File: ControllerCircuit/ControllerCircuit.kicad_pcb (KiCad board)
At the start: 2 copper layers, 122.5 x 87.5 mm, 89 parts, among them J1 ScrewTerminal, J10 Conn_01x02_Female, J11 Conn_01x03_Female, J12 ScrewTerminal, J13 Conn_01x03_Female, J14 Receive, J2 ScrewTerminal3Pin, J3 ScrewTerminal3Pin, J4 ScrewTerminal, J5 ScrewTerminal, J6 AVR-ISP-6, J7 ScrewTerminal, J8 2x3 2.54mm IDC Connectors, J9 Conn_01x06_Female, K1 SRD-05VDC-SL-C, K2 SRD-05VDC-SL-C, Q1 AO3400A, Q2 AO3400A, Q3 AO3401A, SW1 PTS645SL50-2LFS, U1 TJA1051T/3, U10 ATtiny841-SSU, U11 MicroSD_SPI_CD, U12 AQY212GSZ, U2 EL3H7(B)(TA)-G, U3 TCA6408AQPWRQ1, U4 ESP32-DEVKITC-32D, U5 SN65HVD75DR, U6 AMS1117-3.3, U8 TCA9534A, U9 AQY212GSZ

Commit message: Move LEDs near relays (improve seperation)
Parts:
- added G***: LOGO, ControllerCircuit:diode_symbol, F.Cu at (158.7, 74.2)
- added G***: LOGO, ControllerCircuit:diode_symbol, F.Cu at (149.1, 72.1)
- added G***: LOGO, ControllerCircuit:diode_symbol, F.Cu at (201.9, 74.9)
- added G***: LOGO, ControllerCircuit:diode_symbol, F.Cu at (200.7, 53.8)
- added G***: LOGO, ControllerCircuit:diode_symbol, F.Cu at (147.9, 53.7)
- moved R12 36.6 mm to (208.3, 76.1), turned to 180 degrees
- moved D3 19.5 mm to (198.6, 53.6), turned to 90 degrees
- moved R13 6.10 mm to (152.6, 52.9)
- moved D4 1.97 mm to (145.8, 53.6), turned to 90 degrees
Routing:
- net Net-(D3-Pad2): track 4.07 -> 33.2 mm
- net Net-(D2-Pad2): track 49.0 -> 24.2 mm
- net FUSED5V: track 299.4 -> 275.7 mm
- net Net-(D4-Pad1): track 26.8 -> 28.7 mm
- net Net-(D4-Pad2): track 4.45 -> 5.95 mm
- net GND: vias 243 -> 246
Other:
- outline, holes or cut-outs redrawn

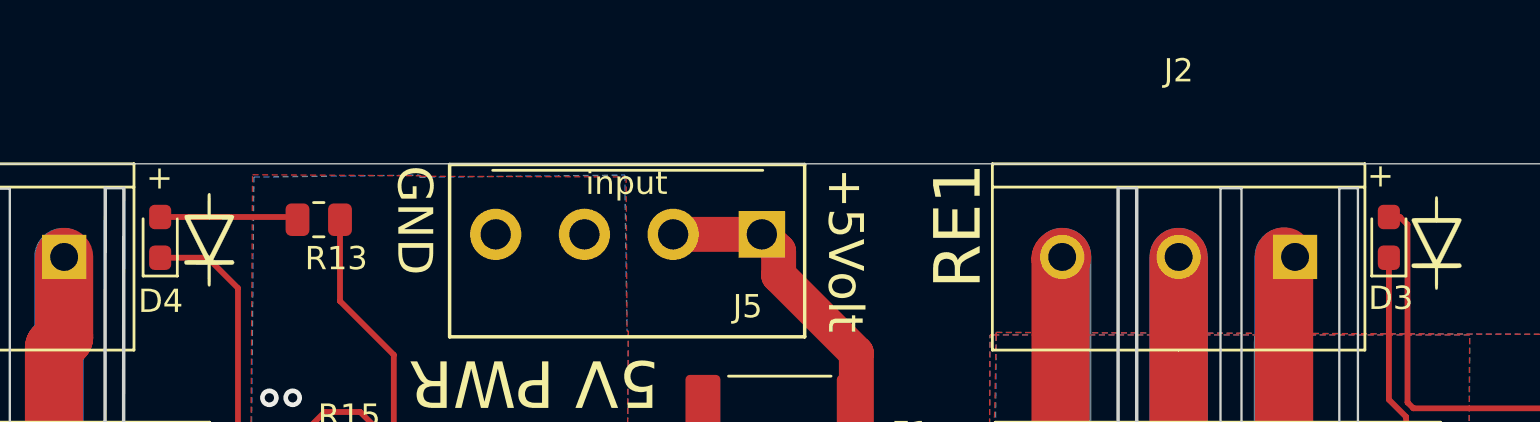
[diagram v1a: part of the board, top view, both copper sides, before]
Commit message: Updated Patreon list on silkscreen
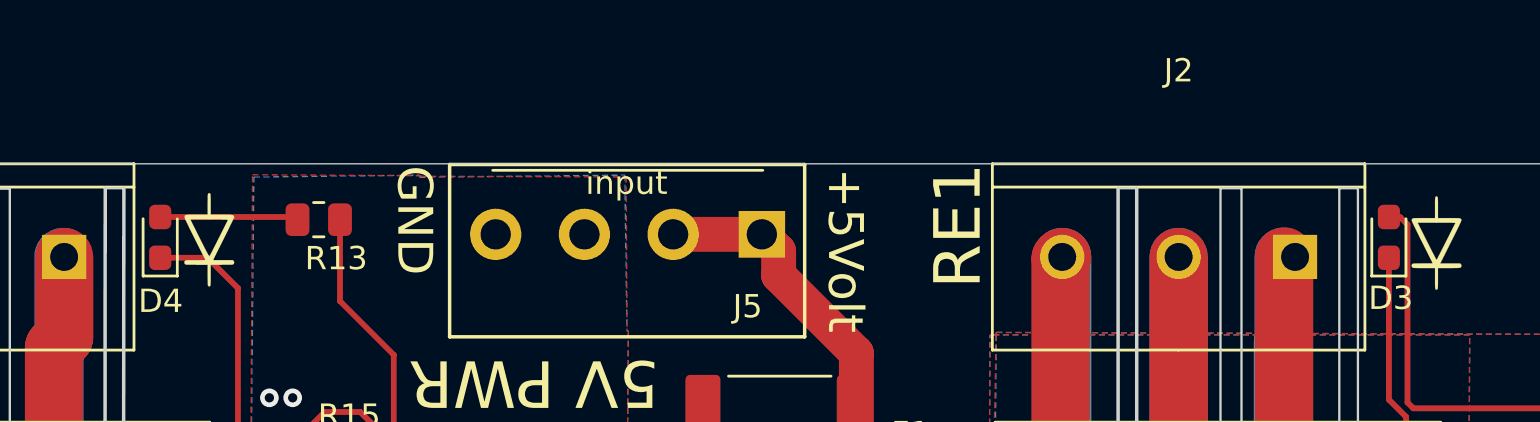
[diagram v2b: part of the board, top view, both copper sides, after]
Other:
- board text added: "IronXSide, Pawel S, Luke Anderson Mukunda Modell, Ken Lyman DIY Solar Energy, Jaanus Marko Kranjcic, Ross Mitchell Micah Peterson, Sebastian M Tim Yorba, chapulino1000 Tudor Bogdan Teodorescu manuromero05, Patrick Murphy Juan Matos, Nico F Arkadiusz Poscik, Marco Martin Bogomolni Julius Pabrinkis Constantine Macris Jose Cruz, Buenaventura Satorra Juanmijm, Thomas W Alberto Santos, Chad Artiaga Th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"
- board text added: "https://github.com/stuartpittaway/diyBMSv4"
- board text removed: "Arkadiusz Poscik, Marco Martin Bogomolni Julius Pabrinkis, Patrick Murphy Constantine Macris Jose Cruz, Juanmijm Buenaventura Satorra Thomas W, Alberto Santos Chad Artiaga, Thales of Miletus manuromero05, Julian Cox"
- board text removed: "IronXSide Pawel S Luke Anderson Mukunda Modell Adam Davis, Ken Lyman DIY Solar Energy Jaanus, Marko Kranjcic Ross Mitchell, Micah Peterson Sebastian M, chapulino1000 Tudor Bogdan Teodorescu Manuel Romero, Tim Yorba Juan Matos, Nico F"
- board text removed: "github.com/stuartpittaway/diyBMSv4Hardware"
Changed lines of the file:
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@@
   (general
     (thickness 1.6)
-    (drawings 188)
+    (drawings 185)
     (tracks 1521)
     (zones 0)
@@
     (34 B.Paste user hide)
     (35 F.Paste user hide)
-    (36 B.SilkS user hide)
+    (36 B.SilkS user)
     (37 F.SilkS user)
     (38 B.Mask user hide)
@@
   (gr_line (start 180.53 78.78) (end 201.99 78.78) (layer B.SilkS) (width 0.12))
   (gr_line (start 180.53 50.8) (end 180.53 78.78) (layer B.SilkS) (width 0.12))
-  (gr_text "Arkadiusz Poscik, Marco\nMartin Bogomolni\n\n\nJulius Pabrinkis, Patrick Murphy\nConstantine Macris\n\n\nJose Cruz, Juanmijm\nBuenaventura Satorra\nThomas W, Alberto Santos\nChad Artiaga, Thales of Miletus\nmanuromero05, Julian Cox" (at 183.7 101.7 90) (layer B.SilkS)
-    (effects (font (size 1.9 1.9) (thickness 0.25)) (justify mirror))
-  )
   (gr_text "\n\n\n\n\n\n\n\n\n\n\n\n\n\n\n\n\n\n\n\n\n\n" (at 159.54 109.71 90) (layer B.SilkS)
     (effects (font (size 2 2) (thickness 0.3)) (justify left mirror))
   )
-  (gr_text "IronXSide\n\nPawel S\nLuke Anderson\nMukunda Modell\nAdam Davis, Ken Lyman\nDIY Solar Energy\nJaanus, Marko Kranjcic\nRoss Mitchell, Micah Peterson\nSebastian M, chapulino1000\nTudor Bogdan Teodorescu\nManuel Romero, Tim Yorba\nJuan Matos, Nico F\n" (at 140.6 101.45 90) (layer B.SilkS)
-    (effects (font (size 1.9 1.9) (thickness 0.25)) (justify mirror))
+  (gr_text "IronXSide, Pawel S, Luke Anderson\n\n\nMukunda Modell, Ken Lyman\n\nDIY Solar Energy, Jaanus\nMarko Kranjcic, Ross Mitchell\nMicah Peterson, Sebastian M\nTim Yorba, \nchapulino1000\nTudor Bogdan Teodorescu\nmanuromero05, Patrick Murphy\nJuan Matos, Nico F\nArkadiusz Poscik, Marco\nMartin Bogomolni\nJulius Pabrinkis\nConstantine Macris\nJose Cruz, Buenaventura Satorra\nJuanmijm, Thomas W\nAlberto Santos, Chad Artiaga\nThales of Miletus, Julian Cox\nOdysseas Sourailidis\nNelson Nunes, Jorge Ramirez\n\nCole Shatto,        Tim Kelley\nPatrick Fischer\nvferrandobe, Andre Borrelly\nJose Pablo Luengo Navas\n\n\nChristopher Ryan\nKeith Chiem, Marc Floyd\nLu Trinh, DIY Tech & Repairs\nFred Moffatt, Jay Brown\nFatai Fashola, Mads Hansen\nChijioke Elijah, Bernd Vollbrecht\nHue, Steve Archibald" (at 158.4 82.75 90) (layer B.SilkS)
+    (effects (font (size 1.5 1.5) (thickness 0.18)) (justify left mirror))
   )
   (gr_line (start 111.37 63.01) (end 103.74 63.01) (layer B.SilkS) (width 0.12))
@@
     (effects (font (size 1 1) (thickness 0.15)))
   )
-  (gr_text + (at 145.78 51.05) (layer F.SilkS)
-    (effects (font (size 1 1) (thickness 0.15)))
-  )
-  (gr_text + (at 198.22 50.96) (layer F.SilkS)
-    (effects (font (size 1 1) (thickness 0.15)))
-  )
   (gr_text "ESP USB SOCKET" (at 109.47 117.52) (layer F.SilkS)
     (effects (font (size 1 1) (thickness 0.15)) (justify right))
@@
     (effects (font (size 1 1) (thickness 0.15)))
   )
-  (gr_text github.com/stuartpittaway/diyBMSv4Hardware (at 158.5 125.27) (layer B.SilkS)
+  (gr_text https://github.com/stuartpittaway/diyBMSv4 (at 158.5 125.27) (layer B.SilkS)
     (effects (font (size 1.5 1.5) (thickness 0.15)) (justify mirror))
   )

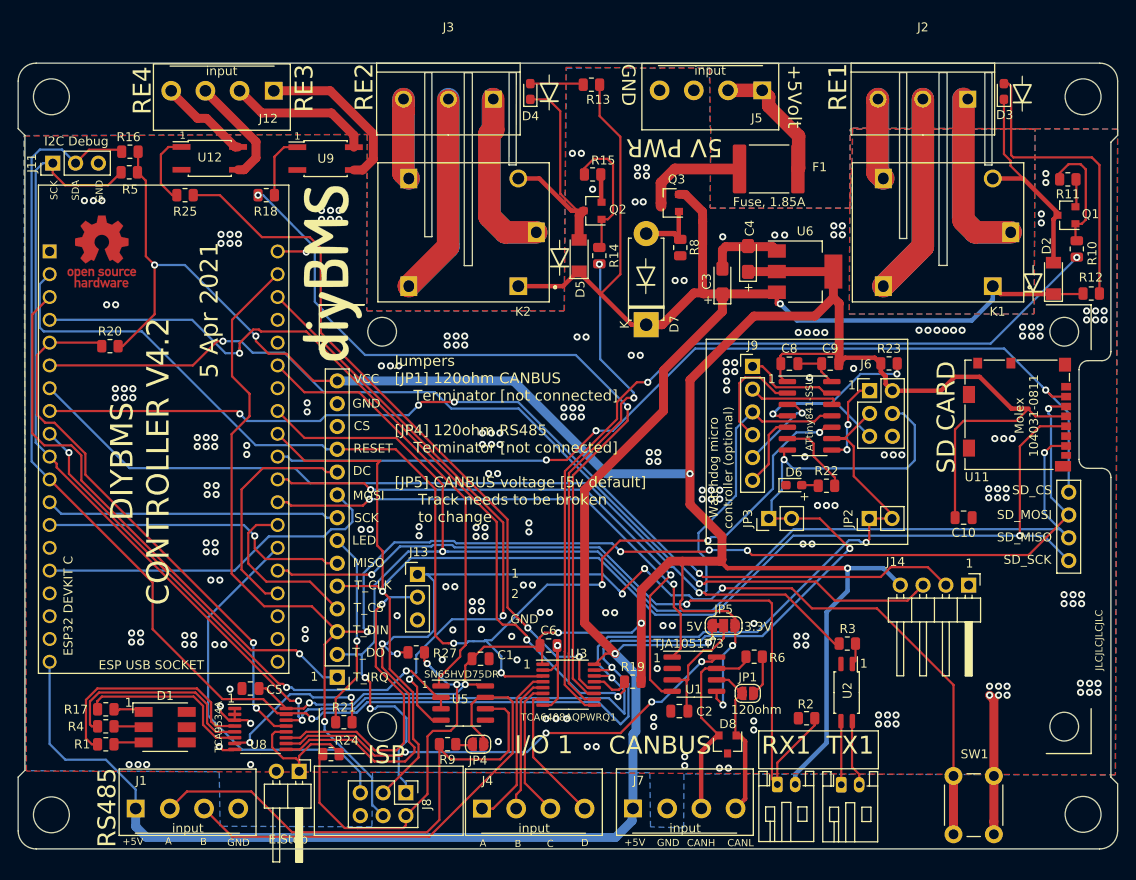
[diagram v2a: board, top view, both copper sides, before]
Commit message: Issue #78 swap of TCA6408APWR
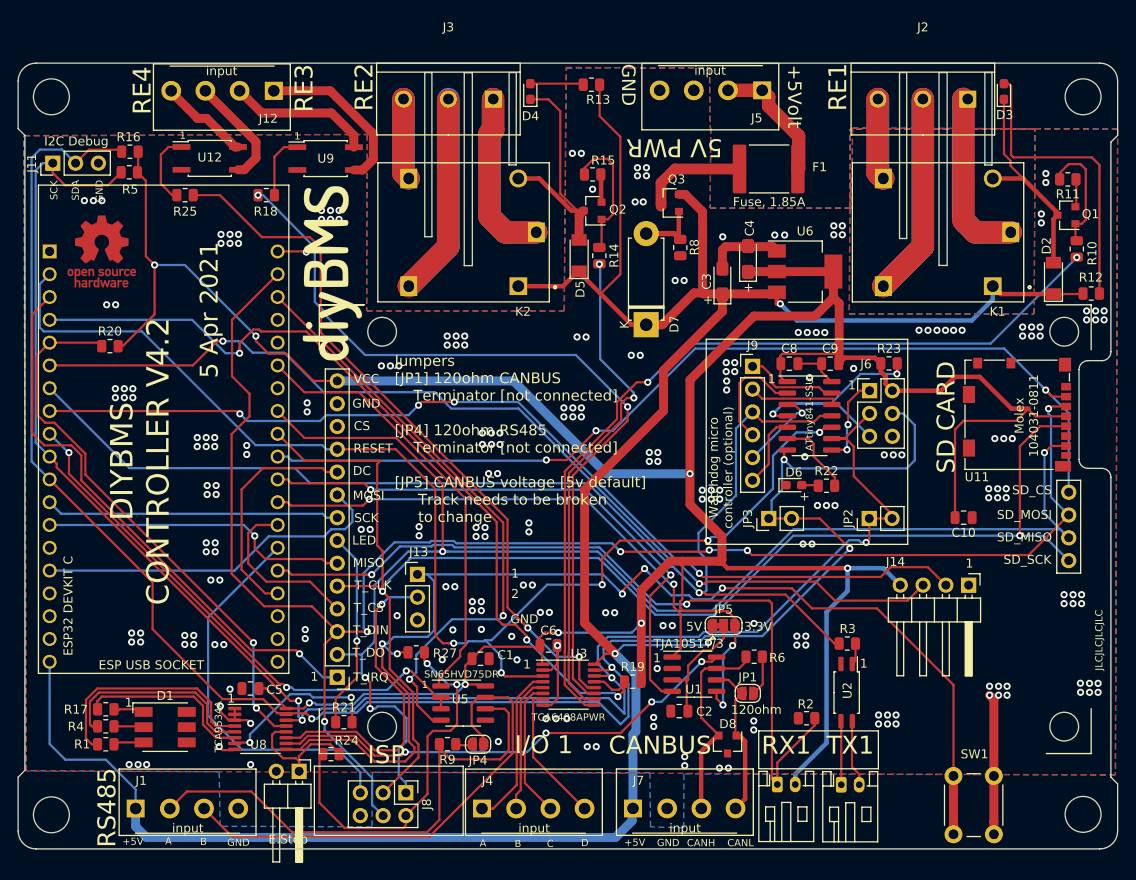
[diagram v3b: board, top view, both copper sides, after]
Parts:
- removed the G*** at (158.7, 74.2)
- removed the G*** at (149.1, 72.1)
- removed the G*** at (201.9, 74.9)
- removed the G*** at (200.7, 53.8)
- removed the G*** at (147.9, 53.7)
- U3: value TCA6408AQPWRQ1 -> TCA6408APWR

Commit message: Added SW1 and SW2 to replace J13
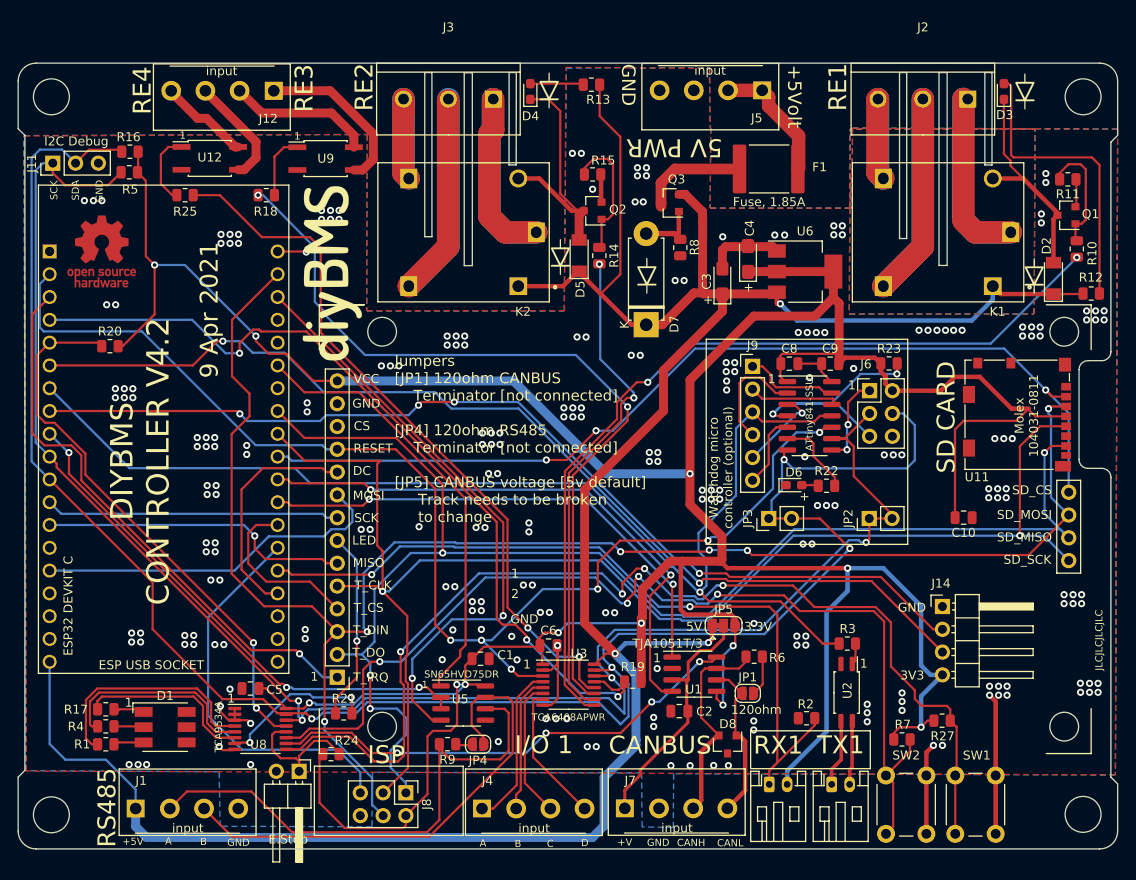
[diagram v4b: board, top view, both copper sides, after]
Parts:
- removed J13: Conn_01x03_Female, Connector_PinHeader_2.54mm:PinHeader_1x03_P2.54mm_Vertical
- added G***: LOGO, ControllerCircuit:diode_symbol, F.Cu at (158.8, 74.1)
- added G***: LOGO, ControllerCircuit:diode_symbol, F.Cu at (149.2, 72.0)
- added G***: LOGO, ControllerCircuit:diode_symbol, F.Cu at (202.0, 74.2)
- added G***: LOGO, ControllerCircuit:diode_symbol, F.Cu at (200.9, 53.6)
- added G***: LOGO, ControllerCircuit:diode_symbol, F.Cu at (147.9, 53.5)
- added R7: 10K, Resistor_SMD:R_0805_2012Metric, F.Cu at (187.2, 125.8)
- added SW2: PTS645SL50-2LFS, Button_Switch_THT:SW_PUSH_6mm_H4.3mm, F.Cu at (185.4, 136.3)
- moved R27 59.1 mm to (191.7, 123.7), turned to 180 degrees
- moved J14 3.77 mm to (191.7, 111.0), turned to 0 degrees
- moved TX1 1.07 mm to (179.4, 130.8)
- moved R21 0.98 mm to (125.0, 122.9)
- moved J7 0.91 mm to (160.2, 133.5)
- moved RX1 0.90 mm to (172.4, 130.8)
- moved SW1 0.21 mm to (193.2, 136.3)
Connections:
- J7 pad 1: FUSED5V -> Net-(C2-Pad1)
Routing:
- net Net-(R7-Pad1): track 35.8 -> 113.5 mm, vias 1 -> 4
- net +3V3: track 404.8 -> 424.9 mm
- net Net-(C2-Pad1): track 13.6 -> 27.6 mm
- net Net-(R27-Pad1): track 131.0 -> 120.1 mm, vias 5 -> 4
- net GND: track 60.6 -> 71.1 mm, vias 246 -> 242
- net /IO35_INPUT: track 111.3 -> 115.3 mm
- net /RESET: track 141.9 -> 140.3 mm, vias 5 -> 6
- net /IO2: track 89.2 -> 87.5 mm
- net /IO25: track 60.0 -> 58.4 mm
- net FUSED5V: track 275.7 -> 274.2 mm
- net /DISPLAY_LED: track 18.8 -> 17.8 mm
- net Net-(LCD1-Pad7): track 22.1 -> 21.2 mm
- net /VSPI_MISO: track 160.0 -> 160.8 mm
- net /VSPI_CLK: track 160.5 -> 159.6 mm
- net /IO33: track 110.5 -> 111.3 mm
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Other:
- board text added: "+V"
- board text added: "3V3"
- board text added: "9 Apr 2021"
- board text removed: "5 Apr 2021"

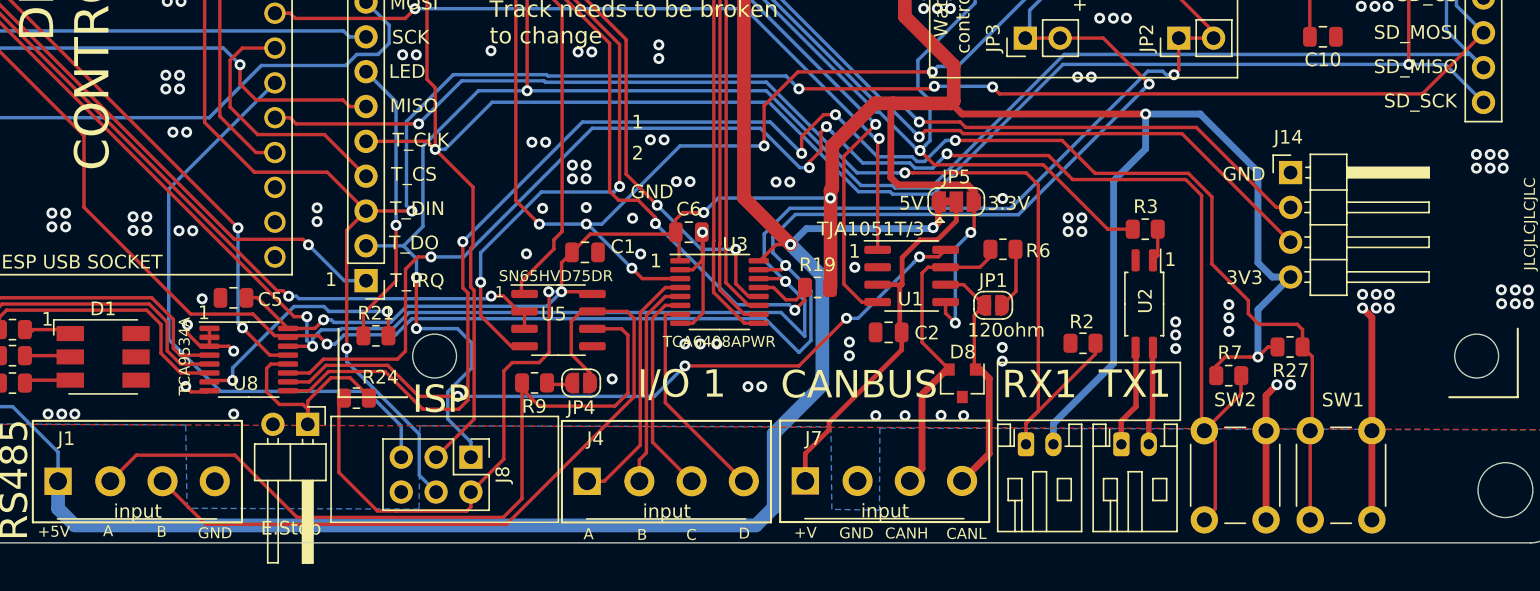
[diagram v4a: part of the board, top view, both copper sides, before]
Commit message: Added SW1 and SW2
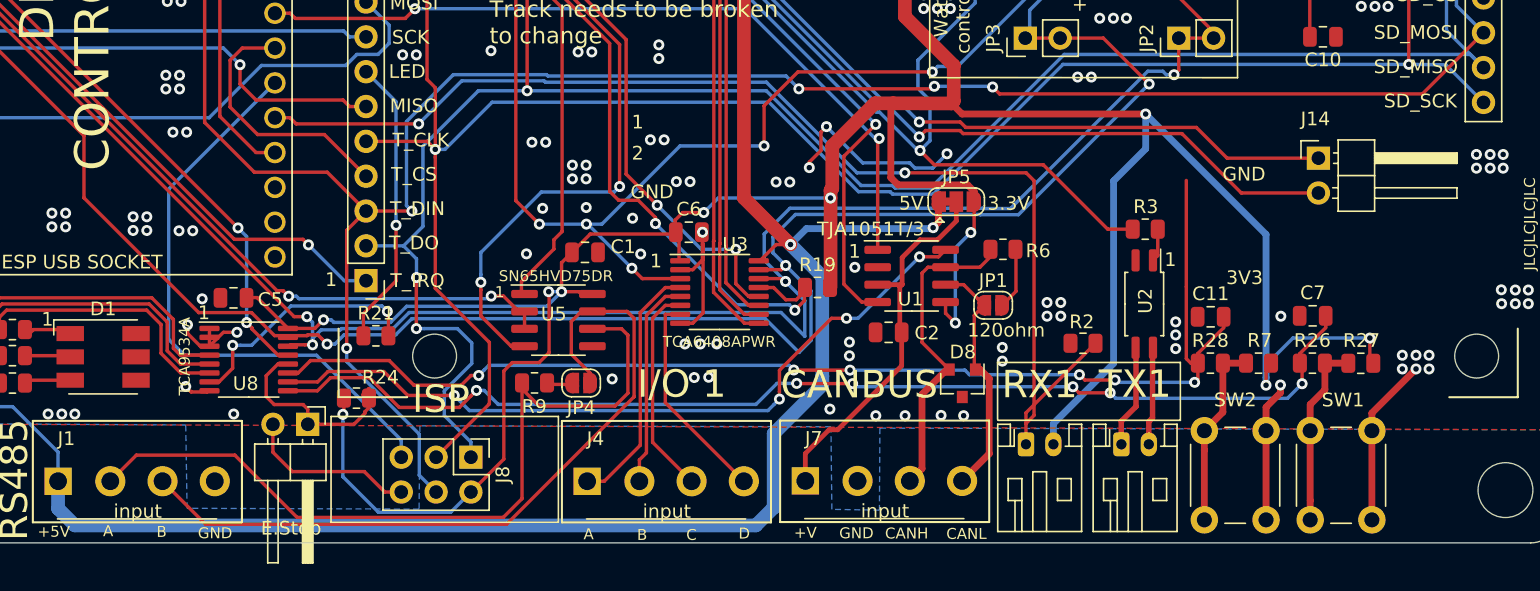
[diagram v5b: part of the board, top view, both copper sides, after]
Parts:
- added C11: 1uF, Capacitor_SMD:C_0805_2012Metric, F.Cu at (185.9, 121.5)
- added C7: 1uF, Capacitor_SMD:C_0805_2012Metric, F.Cu at (193.3, 121.4)
- added R26: 22K, Resistor_SMD:R_0805_2012Metric, F.Cu at (193.3, 124.9)
- added R28: 22K, Resistor_SMD:R_0805_2012Metric, F.Cu at (185.9, 124.9)
- J14: footprint Connector_PinHeader_2.54mm:PinHeader_1x04_P2.54mm_Horizontal -> Connector_PinHeader_2.54mm:PinHeader_1x02_P2.54mm_Horizontal
- R27, R7: value 10K -> 51K
- moved R27 5.30 mm to (196.8, 124.9)
- moved R7 2.35 mm to (189.4, 124.9)
- moved J14 2.29 mm to (193.8, 109.9)
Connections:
- J14 pad 1: GND -> /IO33
- J14 pad 2: /IO33 -> /IO35_INPUT
- R27 pad 1: Net-(R27-Pad1) -> +3V3
- R27 pad 2: +3V3 -> Net-(R26-Pad2)
- R7 pad 1: Net-(R7-Pad1) -> +3V3
- R7 pad 2: +3V3 -> Net-(R28-Pad2)
- SW1 pad 1: Net-(R27-Pad1) -> Net-(R26-Pad2)
- SW2 pad 1: Net-(R7-Pad1) -> Net-(R28-Pad2)
- U8 pad 11: Net-(R7-Pad1) -> /SW2OUTPUT
- U8 pad 9: Net-(R27-Pad1) -> /SW1OUTPUT
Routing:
- net Net-(R27-Pad1): track 120.1 -> 0.00 mm, vias 4 -> 0
- net Net-(R7-Pad1): track 113.5 -> 14.2 mm, vias 4 -> 3
- net /SW2OUTPUT: track 0.00 -> 88.0 mm, vias 0 -> 6
- net /SW1OUTPUT: track 0.00 -> 83.5 mm, vias 0 -> 6
- net Net-(R28-Pad2): track 0.00 -> 13.7 mm
- net Net-(R26-Pad2): track 0.00 -> 13.6 mm
- net GND: track 71.1 -> 81.0 mm, vias 242 -> 237
- net +3V3: track 424.9 -> 429.5 mm, vias 12 -> 14
- net /CANBUS_S: track 53.7 -> 55.4 mm
- net /VSPI_CLK: track 159.6 -> 160.4 mm
- net /AVRISP_RESET: track 43.8 -> 43.2 mm
- net /IO35_INPUT: track 115.3 -> 115.9 mm
- net /IO33: track 111.3 -> 111.8 mm
